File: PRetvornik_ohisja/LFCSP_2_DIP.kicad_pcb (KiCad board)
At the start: 2 copper layers, 3 parts, among them P1 CONN_01X08, P2 CONN_01X08, U1 ADCMP572

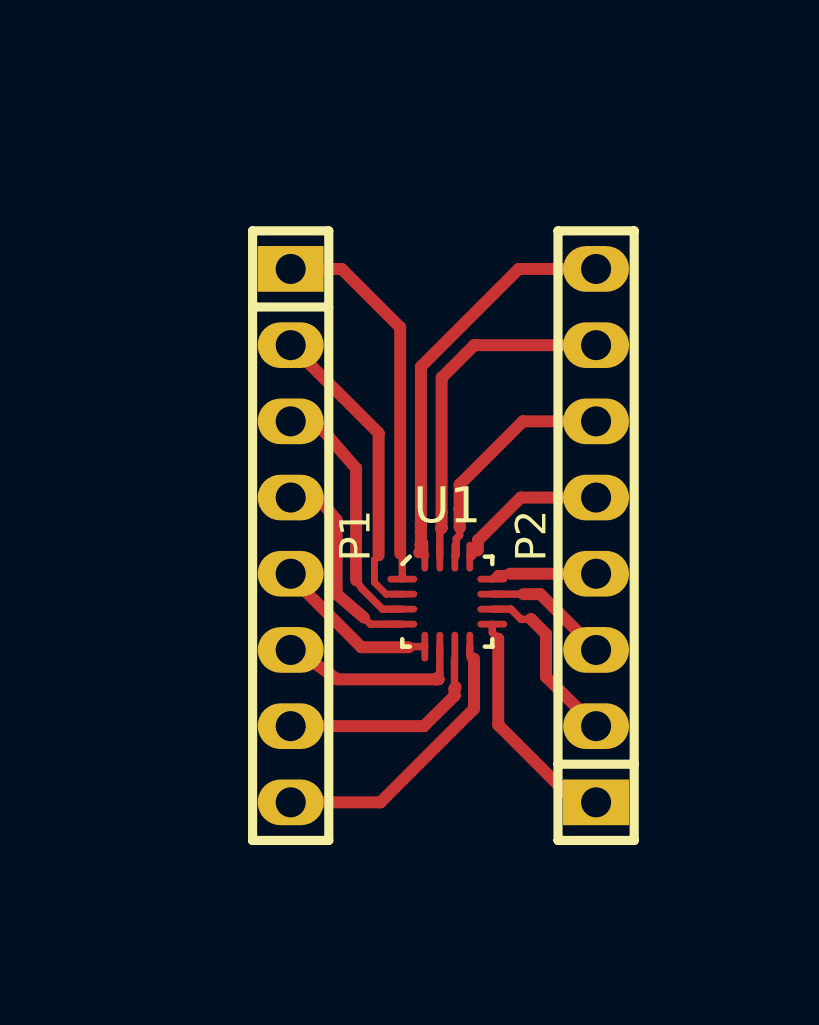
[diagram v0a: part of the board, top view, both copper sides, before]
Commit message: Naredil nov LFCSP s osrednjim padom in ga zavrtel za 45 stopinj
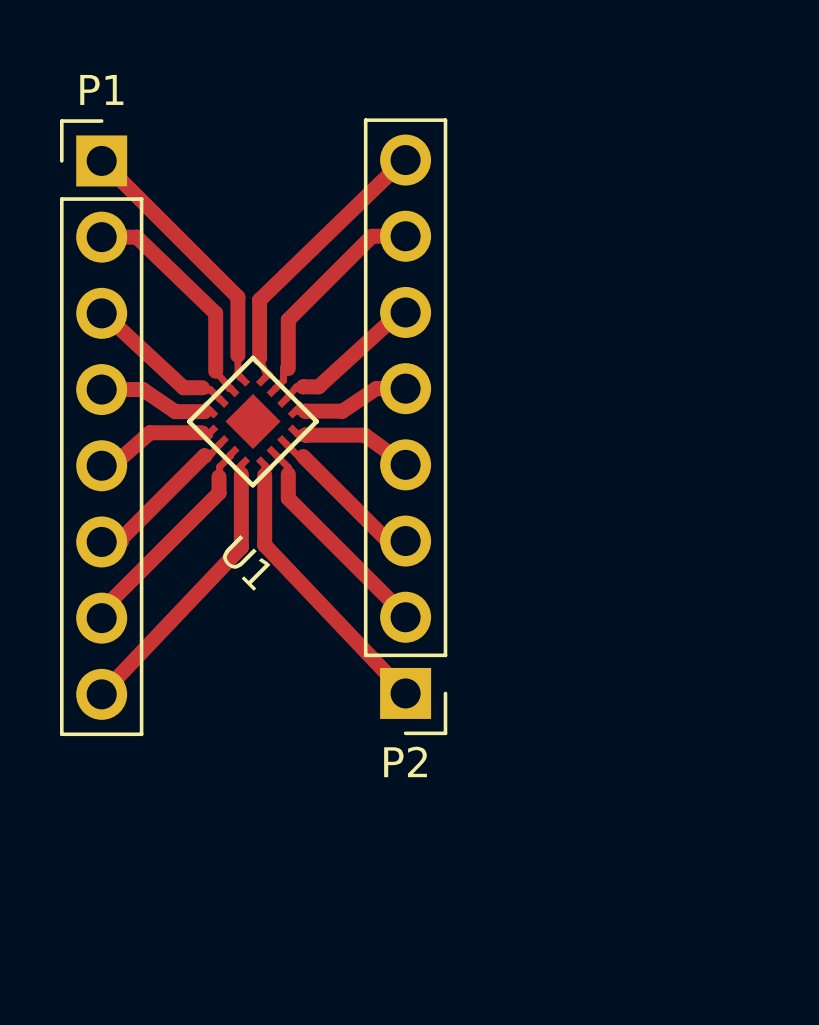
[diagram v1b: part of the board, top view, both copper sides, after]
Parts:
- P1, P2: footprint w_pin_strip:pin_socket_8 -> Socket_Strips:Socket_Strip_Straight_1x08_Pitch2.54mm
- U1: footprint mitja:QFP_16 -> LFCSP:LFCSP_45
- moved P1 14.0 mm to (14.0, 14.0), turned to 0 degrees
- moved U1 8.83 mm to (19.1, 22.6), turned to 315 degrees
- moved P2 8.25 mm to (24.1, 31.8), turned to 180 degrees
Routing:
- net /16: track 14.2 -> 9.61 mm
- net /15: track 11.6 -> 7.51 mm
- net /1: track 12.9 -> 9.39 mm
- net /3: track 8.59 -> 5.13 mm
- net /4: track 6.92 -> 3.84 mm
- net /14: track 7.94 -> 5.16 mm
- net /2: track 10.3 -> 7.60 mm
- net /9: track 7.77 -> 9.51 mm
- net /5: track 5.55 -> 4.14 mm
- net /10: track 5.92 -> 7.27 mm
- net /13: track 5.22 -> 3.96 mm
- net /11: track 4.27 -> 5.52 mm
- net /6: track 6.66 -> 6.04 mm
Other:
- net class Default: trace_width 0.4 -> 0.23
- net class NOrm added: clearance 0.2, trace_width 0.5, via_dia 0.6, via_drill 0.4
